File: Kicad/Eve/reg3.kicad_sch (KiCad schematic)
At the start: 11 parts, among them J5 Conn_01x03, J7 Conn_01x03

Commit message: updtated Kicad ver 7.11.23
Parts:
- removed C10: 10n, Capacitor_SMD:C_0603_1608Metric_Pad1.08x0.95mm_HandSolder, symbol Device:C_Small
- removed C11: 470uF, Capacitor_SMD:CP_Elec_10x10.5, symbol Device:C_Polarized_Small
- removed C9: 220uF, Capacitor_SMD:CP_Elec_10x10.5, symbol Device:C_Polarized_Small
- removed CR3: DST10100S, libs:DST10100S, symbol 2023-03-19_11-33-54:DST10100S
- removed J5, J7: Conn_01x03, symbol Connector_Generic:Conn_01x03
- removed L2: 22uH, Inductor_SMD:L_Wuerth_WE-PD-Typ-LS_Handsoldering, symbol Device:L_Small
- removed R11: 2.7k, Resistor_SMD:R_0603_1608Metric_Pad0.98x0.95mm_HandSolder, symbol Device:R_Small
- removed U10: ~, libs:LT1076CR-PBF, symbol custom:LT1076
- added C6: 220uF, Capacitor_SMD:CP_Elec_10x10.5, symbol Device:C_Polarized_Small
- added C7: 10n, Capacitor_SMD:C_0603_1608Metric_Pad1.08x0.95mm_HandSolder, symbol Device:C_Small
- added C8: 470uF, Capacitor_SMD:CP_Elec_10x10.5, symbol Device:C_Polarized_Small
- added CR1: DST10100S, TO277B_LTF, symbol 2023-03-19_11-33-54:DST10100S
- added D3: LED, LED_SMD:LED_0603_1608Metric_Pad1.05x0.95mm_HandSolder, symbol Device:LED
- added L1: 22uH, Inductor_SMD:L_Wuerth_WE-PD-Typ-LS_Handsoldering, symbol Device:L_Small
- added R4: 1k, Resistor_SMD:R_0603_1608Metric_Pad0.98x0.95mm_HandSolder, symbol Device:R_Small
- added R8: 2.7k, Resistor_SMD:R_0603_1608Metric_Pad0.98x0.95mm_HandSolder, symbol Device:R_Small
- added U1: ~, symbol custom:LT1076
- R12: value 40k -> 43k
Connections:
- net GND: now also C6.2, C7.2, C8.2, CR1.1, CR1.2, D3.1 (K), U1.4 (GND)
- net Vsw: now also CR1.3, L1.1, U1.2 (Vsw)
- net at R12.2, R13.1: now also U1.5 (FB)
- net 11.1V renamed 11.7V
- net 11.7V: now also C8.1, L1.2, R4.1
- new net: D3.2 (A), R4.2
- new net: C7.1, R8.2
- new net: R8.1, U1.6 (Vc)
- new net 24V: C6.1, U1.1 (Vin), U1.7 (Shutdown)
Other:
- moved on the sheet: R13

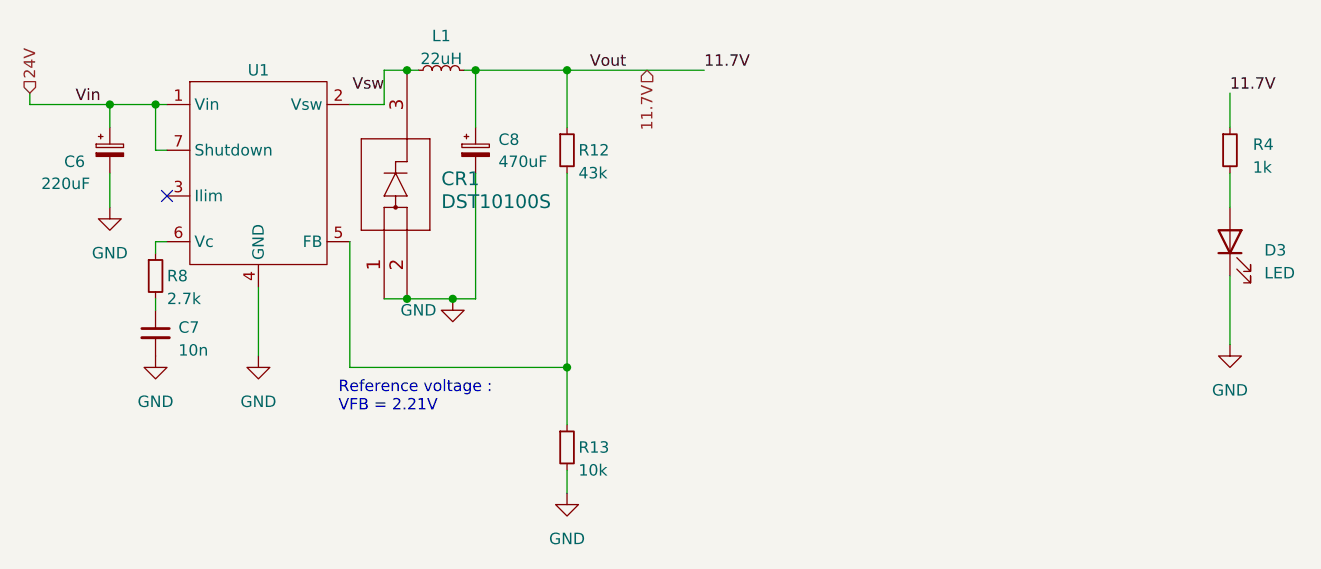
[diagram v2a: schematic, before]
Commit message: added Kicad libraries to git + sch changes 11/11/23
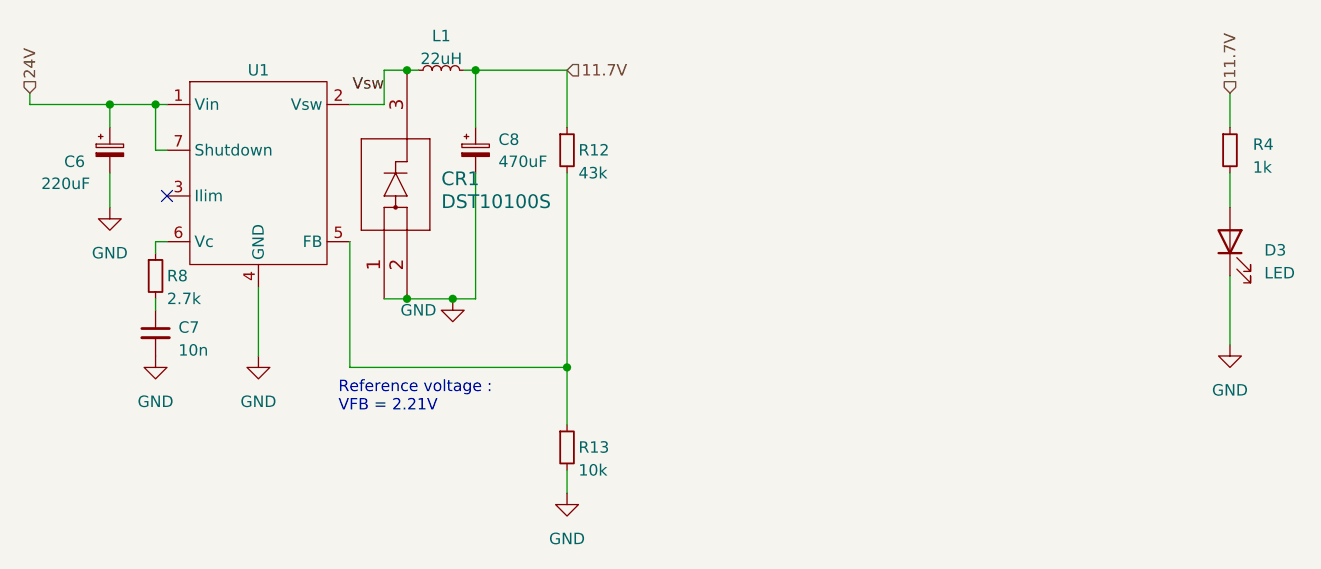
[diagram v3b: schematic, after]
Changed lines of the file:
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@@
   (junction (at 110.49 80.01) (diameter 0) (color 0 0 0 0)
-  )
-  (junction (at 156.21 76.2) (diameter 0) (color 0 0 0 0)
   )
   (junction (at 138.43 76.2) (diameter 0) (color 0 0 0 0)
@@
     (stroke (width 0) (type default))
   )
-  (wire (pts (xy 156.21 76.2) (xy 171.45 76.2))
-    (stroke (width 0) (type default))
-  )
   (wire (pts (xy 156.21 76.2) (xy 156.21 82.55))
     (stroke (width 0) (type default))
@@
     (effects (font (size 1.27 1.27)) (justify left bottom))
   )
-  (label "Vin" (at 101.6 80.01 0) (fields_autoplaced)
-    (effects (font (size 1.27 1.27)) (justify left bottom))
-  )
   (label "Vsw" (at 135.89 78.74 180) (fields_autoplaced)
     (effects (font (size 1.27 1.27)) (justify right bottom))
   )
-  (label "11.7V" (at 171.45 76.2 0) (fields_autoplaced)
-    (effects (font (size 1.27 1.27)) (justify left bottom))
+  (hierarchical_label "11.7V" (shape input) (at 229.87 78.74 90) (fields_autoplaced)
+    (effects (font (size 1.27 1.27)) (justify left))
   )
-  (label "11.7V" (at 229.87 78.74 0) (fields_autoplaced)
-    (effects (font (size 1.27 1.27)) (justify left bottom))
-  )
-  (label "Vout" (at 158.75 76.2 0) (fields_autoplaced)
-    (effects (font (size 1.27 1.27)) (justify left bottom))
-  )
-  (hierarchical_label "11.7V" (shape input) (at 165.1 76.2 270) (fields_autoplaced)
-    (effects (font (size 1.27 1.27)) (justify right))
+  (hierarchical_label "11.7V" (shape input) (at 156.21 76.2 0) (fields_autoplaced)
+    (effects (font (size 1.27 1.27)) (justify left))
   )
   (hierarchical_label "24V" (shape input) (at 96.52 78.74 90) (fields_autoplaced)

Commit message: empreinte 13/11
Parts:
- C6: value 220uF -> 220u; footprint Capacitor_SMD:CP_Elec_10x10.5 -> (none)
- C8: value 470uF -> 470u; footprint Capacitor_SMD:CP_Elec_10x10.5 -> (none)
- CR1: footprint TO277B_LTF -> libs:DST10100S
- L1: footprint Inductor_SMD:L_Wuerth_WE-PD-Typ-LS_Handsoldering -> (none)
- U1: footprint (none) -> libs:LT1076CR-PBF
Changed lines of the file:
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@@
       (effects (font (size 1.27 1.27)))
     )
-    (property "Footprint" "Inductor_SMD:L_Wuerth_WE-PD-Typ-LS_Handsoldering" (at 142.24 76.2 0)
+    (property "Footprint" "" (at 142.24 76.2 0)
       (effects (font (size 1.27 1.27)) hide)
     )
@@
       (effects (font (size 1.524 1.524)) (justify right))
     )
-    (property "Footprint" "TO277B_LTF" (at 132.334 88.9 0)
+    (property "Footprint" "libs:DST10100S" (at 132.334 88.9 0)
       (effects (font (size 1.524 1.524)) hide)
     )
@@
       (effects (font (size 1.27 1.27)) (justify left))
     )
-    (property "Value" "220uF" (at 97.79 88.8111 0)
-      (effects (font (size 1.27 1.27)) (justify left))
-    )
-    (property "Footprint" "Capacitor_SMD:CP_Elec_10x10.5" (at 105.41 85.09 0)
+    (property "Value" "220u" (at 97.79 88.8111 0)
+      (effects (font (size 1.27 1.27)) (justify left))
+    )
+    (property "Footprint" "" (at 105.41 85.09 0)
       (effects (font (size 1.27 1.27)) hide)
     )
@@
       (effects (font (size 1.27 1.27)) (justify left))
     )
-    (property "Value" "470uF" (at 148.59 86.36 0)
-      (effects (font (size 1.27 1.27)) (justify left))
-    )
-    (property "Footprint" "Capacitor_SMD:CP_Elec_10x10.5" (at 146.05 85.09 0)
+    (property "Value" "470u" (at 148.59 86.36 0)
+      (effects (font (size 1.27 1.27)) (justify left))
+    )
+    (property "Footprint" "" (at 146.05 85.09 0)
       (effects (font (size 1.27 1.27)) hide)
     )
@@
       (effects (font (size 1.27 1.27)))
     )
-    (property "Footprint" "" (at 116.84 83.82 0)
-      (effects (font (size 1.27 1.27)) hide)
-    )
+    (property "Footprint" "libs:LT1076CR-PBF" (at 116.84 83.82 0)
+      (effects (font (size 1.27 1.27)) hide)
+    )

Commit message: pulled main and started routing
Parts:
- C6, C8: footprint (none) -> Capacitor_SMD:CP_Elec_10x10.5
- L1: footprint (none) -> Eagle_WE-PD (rev23a):WE-PD_1210
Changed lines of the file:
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@@
       (effects (font (size 1.27 1.27)))
     )
-    (property "Footprint" "" (at 142.24 76.2 0)
+    (property "Footprint" "Eagle_WE-PD (rev23a):WE-PD_1210" (at 142.24 76.2 0)
       (effects (font (size 1.27 1.27)) hide)
     )
@@
       (effects (font (size 1.27 1.27)) (justify left))
     )
-    (property "Footprint" "" (at 105.41 85.09 0)
+    (property "Footprint" "Capacitor_SMD:CP_Elec_10x10.5" (at 105.41 85.09 0)
       (effects (font (size 1.27 1.27)) hide)
     )
@@
       (effects (font (size 1.27 1.27)) (justify left))
     )
-    (property "Footprint" "" (at 146.05 85.09 0)
-      (effects (font (size 1.27 1.27)) hide)
-    )
+    (property "Footprint" "Capacitor_SMD:CP_Elec_10x10.5" (at 146.05 85.09 0)
+      (effects (font (size 1.27 1.27)) hide)
+    )
